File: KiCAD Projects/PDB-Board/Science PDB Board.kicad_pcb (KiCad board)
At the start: 2 copper layers, 85.1 x 63.5 mm, 12 parts, among them P1 MOTOR_PWR_OUT, P2 MAIN_PWR_IN, P3 5V_OUT, P4 PWR_REG

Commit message: Finished working on PDB.
Ready for another review.
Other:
- board text added: "UW Husky Robotics 2017 Cai B. / Jaden B. Sci Power Distribution v1.1"
- board text removed: "UW Husky Robotics 2017 Cai B. / Jaden B. Sci Power Distribution v1"
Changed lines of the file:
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@@
     (effects (font (size 1.5 1.5) (thickness 0.3)) (justify mirror))
   )
-  (gr_text "UW Husky Robotics 2017\nCai B. / Jaden B.\nSci Power Distribution v1" (at 177.165 82.55) (layer F.SilkS)
+  (gr_text "UW Husky Robotics 2017\nCai B. / Jaden B.\nSci Power Distribution v1.1" (at 177.165 82.55) (layer F.SilkS)
     (effects (font (size 1.5 1.5) (thickness 0.3)))
   )

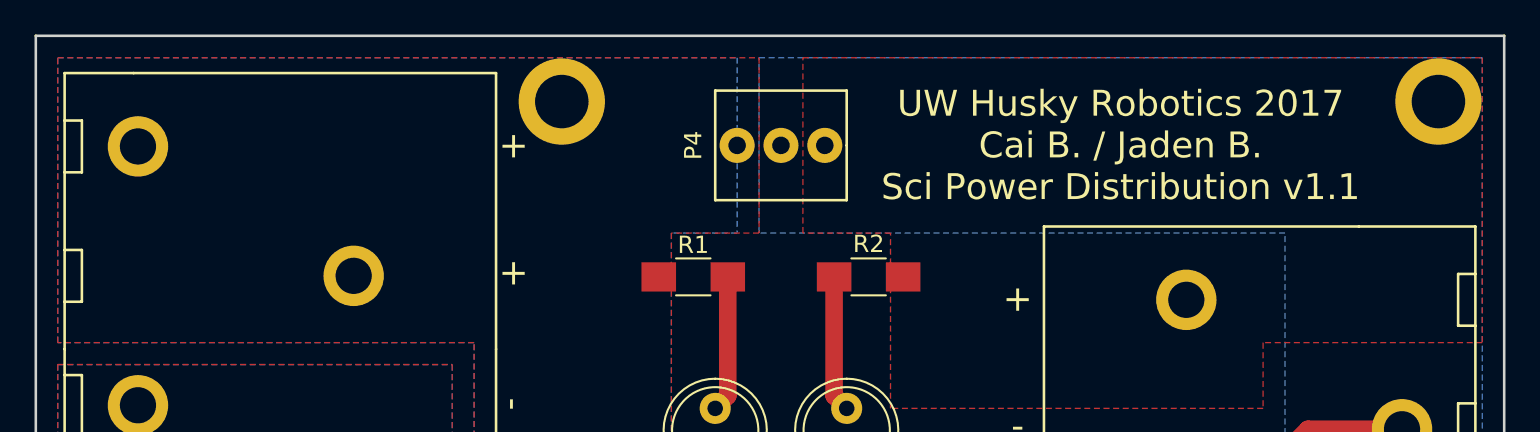
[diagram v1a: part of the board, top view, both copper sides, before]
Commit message: Added Ethernet switch power connector
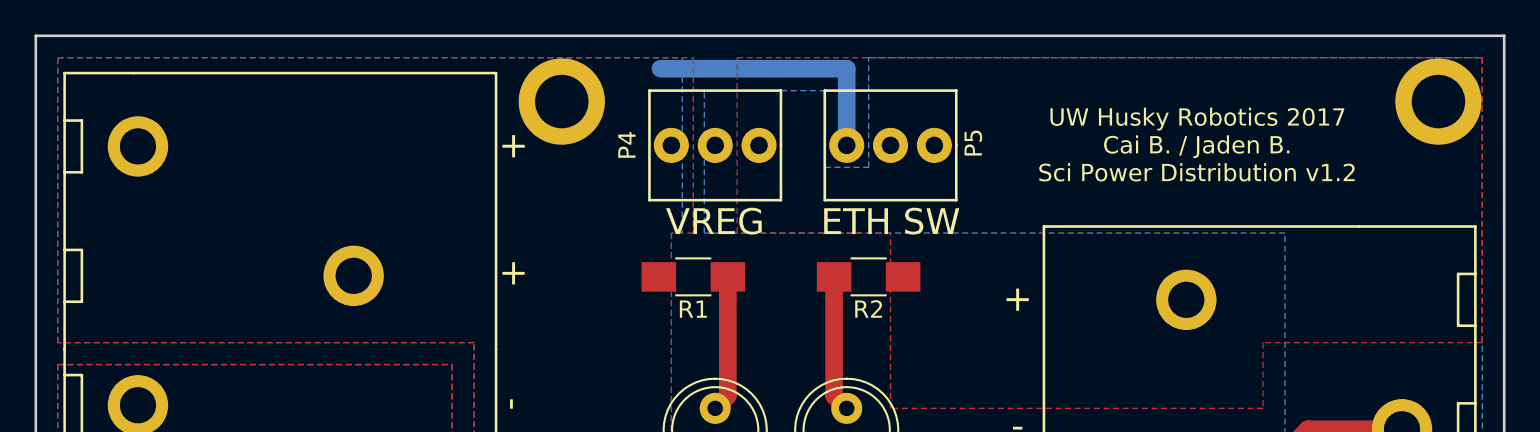
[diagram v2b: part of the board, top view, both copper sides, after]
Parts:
- added P5: ETH_SWITCH, .pretty:MOLEX_0022232031, F.Cu at (163.8, 82.5)
- moved P4 3.81 mm to (153.7, 82.5)
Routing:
- net +12V: track 0.00 -> 15.2 mm
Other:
- rule trace_min: 0.2 -> 0
- board text added: "12V"
- board text added: "5V"
- board text added: "ETH SW"
- board text added: "UW Husky Robotics 2017 Cai B. / Jaden B. Sci Power Distribution v1.2"
- board text added: "VREG"
- board text removed: "UW Husky Robotics 2017 Cai B. / Jaden B. Sci Power Distribution v1.1"
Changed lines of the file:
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@@
 (kicad_pcb (version 4) (host pcbnew 4.0.3-stable)
   (general
-    (links 20)
+    (links 23)
     (no_connects 0)
     (area 114.224999 76.124999 199.465001 139.775001)
     (thickness 1.6)
-    (drawings 33)
-    (tracks 8)
+    (drawings 41)
+    (tracks 10)
     (zones 0)
-    (modules 12)
+    (modules 13)
     (nets 10)
   )
@@
   )
   (setup
-    (last_trace_width 0.25)
+    (last_trace_width 1.016)
     (user_trace_width 1.016)
     (trace_clearance 0.2)
     (zone_clearance 0.508)
     (zone_45_only no)
-    (trace_min 0.2)
+    (trace_min 0)
     (segment_width 0.2)
     (edge_width 0.15)
@@
     (tags "resistor 1206")
     (attr smd)
-    (fp_text reference R1 (at 0 -1.85) (layer F.SilkS)
+    (fp_text reference R1 (at 0 1.905) (layer F.SilkS)
       (effects (font (size 1 1) (thickness 0.15)))
     )
@@
       (effects (font (size 1 1) (thickness 0.15)))
     )
-    (fp_text user %R (at 0 -1.85) (layer F.Fab)
+    (fp_text user %R (at 0 1.905) (layer F.Fab)
       (effects (font (size 1 1) (thickness 0.15)))
     )
@@
     (tags "resistor 1206")
     (attr smd)
-    (fp_text reference R2 (at 0 1.905 360) (layer F.SilkS)
+    (fp_text reference R2 (at 0 -1.905 360) (layer F.SilkS)
       (effects (font (size 1 1) (thickness 0.15)))
     )
@@
       (effects (font (size 1 1) (thickness 0.15)))
     )
-    (fp_text user %R (at 0 1.905 180) (layer F.Fab)
+    (fp_text user %R (at 0 -1.905 180) (layer F.Fab)
       (effects (font (size 1 1) (thickness 0.15)))
     )
@@
   )
   (module .pretty:MOLEX_0022232031 (layer F.Cu)
-    (at 157.48 82.55)
+    (at 153.67 82.55)
     (fp_text reference P4 (at -5.08 0 270) (layer F.SilkS)
       (effects (font (size 1 1) (thickness 0.15)))
@@
       (net 9 "Net-(HL4-Pad1)"))
   )
+  (module .pretty:MOLEX_0022232031 (layer F.Cu)
+    (at 163.83 82.55)
+    (fp_text reference P5 (at 4.826 -0.127 90) (layer F.SilkS)
+      (effects (font (size 1 1) (thickness 0.15)))
+    )
+    (fp_text value ETH_SWITCH (at 0 -4.064) (layer F.Fab)
+      (effects (font (size 1 1) (thickness 0.15)))
+    )
+    (fp_line (start 3.81 0) (end 3.81 3.175) (layer F.SilkS) (width 0.15))
+    (fp_line (start 3.81 3.175) (end -3.81 3.175) (layer F.SilkS) (width 0.15))
+    (fp_line (start -3.81 3.175) (end -3.81 -3.175) (layer F.SilkS) (width 0.15))
+    (fp_line (start -3.81 -3.175) (end 3.81 -3.175) (layer F.SilkS) (width 0.15))
+    (fp_line (start 3.81 -3.175) (end 3.81 0) (layer F.SilkS) (width 0.15))
+    (pad 2 thru_hole circle (at 0 0) (size 2.032 2.032) (drill 1.016) (layers *.Cu *.Mask)
+      (net 5 GND))
+    (pad 1 thru_hole circle (at -2.54 0) (size 2.032 2.032) (drill 1.016) (layers *.Cu *.Mask)
+      (net 1 +12V))
+    (pad 3 thru_hole circle (at 2.54 0) (size 2.032 2.032) (drill 1.016) (layers *.Cu *.Mask)
+      (net 3 +5V))
+  )
+  (gr_text 5V (at 166.37 78.105 90) (layer B.SilkS)
+    (effects (font (size 1 1) (thickness 0.2)) (justify left mirror))
+  )
+  (gr_text GND (at 163.83 78.105 90) (layer B.SilkS)
+    (effects (font (size 1 1) (thickness 0.2)) (justify left mirror))
+  )
+  (gr_text 12V (at 161.29 78.105 90) (layer B.SilkS)
+    (effects (font (size 1 1) (thickness 0.2)) (justify left mirror))
+  )
+  (gr_text 5V (at 156.21 78.105 90) (layer B.SilkS)
+    (effects (font (size 1 1) (thickness 0.2)) (justify left mirror))
+  )
+  (gr_text GND (at 153.67 78.105 90) (layer B.SilkS)
+    (effects (font (size 1 1) (thickness 0.2)) (justify left mirror))
+  )
+  (gr_text 12V (at 151.13 78.105 90) (layer B.SilkS)
+    (effects (font (size 1 1) (thickness 0.2)) (justify left mirror))
+  )
+  (gr_text VREG (at 153.67 86.995) (layer F.SilkS)
+    (effects (font (size 1.5 1.5) (thickness 0.3)))
+  )
+  (gr_text "ETH SW" (at 163.83 86.995) (layer F.SilkS)
+    (effects (font (size 1.5 1.5) (thickness 0.3)))
+  )
   (gr_text +12Vi (at 116.332 82.296 270) (layer B.SilkS)
     (effects (font (size 1.5 1.5) (thickness 0.3)) (justify mirror))
@@
     (effects (font (size 1.5 1.5) (thickness 0.3)) (justify mirror))
   )
-  (gr_text "UW Husky Robotics 2017\nCai B. / Jaden B.\nSci Power Distribution v1.1" (at 177.165 82.55) (layer F.SilkS)
-    (effects (font (size 1.5 1.5) (thickness 0.3)))
+  (gr_text "UW Husky Robotics 2017\nCai B. / Jaden B.\nSci Power Distribution v1.2" (at 181.61 82.55) (layer F.SilkS)
+    (effects (font (size 1 1) (thickness 0.2)))
   )
   (gr_line (start 114.3 139.7) (end 114.3 76.2) (angle 90) (layer Edge.Cuts) (width 0.15))
@@
   (gr_line (start 199.39 76.2) (end 199.39 139.7) (angle 90) (layer Edge.Cuts) (width 0.15))
   (gr_line (start 114.3 76.2) (end 199.39 76.2) (angle 90) (layer Edge.Cuts) (width 0.15))
+  (segment (start 161.29 82.55) (end 161.29 78.105) (width 1.016) (layer B.Cu) (net 1))
+  (segment (start 161.29 78.105) (end 150.495 78.105) (width 1.016) (layer B.Cu) (net 1))
   (segment (start 154.4 90.17) (end 154.4 97.06) (width 1.016) (layer F.Cu) (net 2))
   (segment (start 154.4 97.06) (end 153.67 97.79) (width 1.016) (layer F.Cu) (net 2))
@@
       (pts
         (xy 198.12 93.98) (xy 185.42 93.98) (xy 185.42 97.79) (xy 163.83 97.79) (xy 163.83 87.63)
-        (xy 158.75 87.63) (xy 158.75 77.47) (xy 198.12 77.47)
+        (xy 154.94 87.63) (xy 154.94 77.47) (xy 198.12 77.47)
       )
     )
@@
     (polygon
       (pts
-        (xy 156.21 87.63) (xy 151.13 87.63) (xy 151.13 102.87) (xy 198.12 102.87) (xy 198.12 124.46)
-        (xy 139.7 124.46) (xy 139.7 93.98) (xy 115.57 93.98) (xy 115.57 77.47) (xy 156.21 77.47)
+        (xy 152.4 87.63) (xy 151.13 87.63) (xy 151.13 102.87) (xy 198.12 102.87) (xy 198.12 124.46)
+        (xy 139.7 124.46) (xy 139.7 93.98) (xy 115.57 93.98) (xy 115.57 77.47) (xy 152.4 77.47)
       )
     )
@@
       (pts
         (xy 138.43 125.73) (xy 193.04 125.73) (xy 193.04 114.3) (xy 186.69 114.3) (xy 186.69 87.63)
-        (xy 156.21 87.63) (xy 156.21 77.47) (xy 198.12 77.47) (xy 198.12 138.43) (xy 115.57 138.43)
-        (xy 115.57 95.25) (xy 138.43 95.25)
+        (xy 153.035 87.63) (xy 153.035 79.375) (xy 160.02 79.375) (xy 160.02 83.82) (xy 162.56 83.82)
+        (xy 162.56 77.47) (xy 198.12 77.47) (xy 198.12 138.43) (xy 115.57 138.43) (xy 115.57 95.25)
+        (xy 138.43 95.25)
       )
     )
@@
     (polygon
       (pts
-        (xy 154.94 87.63) (xy 151.13 87.63) (xy 151.13 102.87) (xy 185.42 102.87) (xy 185.42 115.57)
+        (xy 151.765 87.63) (xy 151.13 87.63) (xy 151.13 102.87) (xy 185.42 102.87) (xy 185.42 115.57)
         (xy 191.77 115.57) (xy 191.77 124.46) (xy 139.7 124.46) (xy 139.7 93.98) (xy 115.57 93.98)
-        (xy 115.57 77.47) (xy 154.94 77.47)
+        (xy 115.57 77.47) (xy 151.765 77.47)
       )
     )
